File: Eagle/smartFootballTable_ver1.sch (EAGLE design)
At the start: 22 parts, among them IC1 LM2940CT, K1 ARK500/2

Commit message: Updated board with latest changes after soldering
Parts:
- removed J5: (no value), jumper:J2X2MM
- added JP1: (no value), jumper:JP2W
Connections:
- net +5V: now also JP1.1; no longer J5.1
- net GND: now also JP1.3; no longer J5.3
- net N$31: now also JP1.2; no longer J5.2
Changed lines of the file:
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@@
 </part>
 <part name="ARDUINO_NANO1" library="ArduinoNanoV30" deviceset="ARDUINO_NANO" device=""/>
-<part name="J5" library="jumper" deviceset="J2" device="X2MM"/>
 <part name="DIS_1" library="#PaJa_konektory" deviceset="PSH02-07" device="W"/>
 <part name="DIS_2" library="#PaJa_konektory" deviceset="PSH02-07" device="W"/>
@@
 <part name="TEST" library="#PaJa_prepinace" deviceset="P-B1720" device=""/>
 <part name="J1" library="con-jack" deviceset="JACK-PLUG" device="1"/>
+<part name="JP1" library="jumper" deviceset="JP2W" device=""/>
 </parts>
 <sheets>
@@
 </instance>
 <instance part="ARDUINO_NANO1" gate="G$1" x="-7.62" y="53.34" rot="R180"/>
-<instance part="J5" gate="G$1" x="-20.32" y="10.16" rot="R90"/>
 <instance part="DIS_1" gate="KON" x="55.88" y="71.12" rot="R270"/>
 <instance part="DIS_2" gate="KON" x="55.88" y="35.56" rot="R270"/>
@@
 <instance part="TEST" gate="TLAC" x="27.94" y="12.7"/>
 <instance part="J1" gate="G$1" x="-45.72" y="111.76"/>
+<instance part="JP1" gate="1" x="-20.32" y="10.16"/>
 </instances>
 <busses>
@@
 <wire x1="-12.7" y1="-2.54" x2="-12.7" y2="-5.08" width="0.1524" layer="91"/>
 <wire x1="-12.7" y1="-5.08" x2="-10.16" y2="-5.08" width="0.1524" layer="91"/>
-<pinref part="J5" gate="G$1" pin="3"/>
-<wire x1="-17.78" y1="7.62" x2="-17.78" y2="-5.08" width="0.1524" layer="91"/>
-<junction x="-17.78" y="-5.08"/>
 <pinref part="SENS_2" gate="KON" pin="6"/>
 <pinref part="SENS_2" gate="KON" pin="7"/>
 <junction x="-12.7" y="-5.08"/>
+<pinref part="JP1" gate="1" pin="3"/>
+<wire x1="-17.78" y1="7.62" x2="-17.78" y2="-2.54" width="0.1524" layer="91"/>
+<junction x="-17.78" y="-2.54"/>
 </segment>
 </net>
@@
 <wire x1="-25.4" y1="-2.54" x2="-25.4" y2="5.08" width="0.1524" layer="91"/>
 <wire x1="-25.4" y1="5.08" x2="-22.86" y2="5.08" width="0.1524" layer="91"/>
-<pinref part="J5" gate="G$1" pin="1"/>
-<wire x1="-22.86" y1="5.08" x2="-22.86" y2="7.62" width="0.1524" layer="91"/>
 <wire x1="-35.56" y1="-5.08" x2="-35.56" y2="-2.54" width="0.1524" layer="91"/>
 <wire x1="-35.56" y1="-2.54" x2="-25.4" y2="-2.54" width="0.1524" layer="91"/>
 <junction x="-25.4" y="-2.54"/>
 <pinref part="SENS_1" gate="KON" pin="1"/>
+<pinref part="JP1" gate="1" pin="1"/>
+<wire x1="-22.86" y1="5.08" x2="-22.86" y2="7.62" width="0.1524" layer="91"/>
 </segment>
 </net>
@@
 <pinref part="R3" gate="G$1" pin="2"/>
 <pinref part="R4" gate="G$1" pin="2"/>
-<wire x1="-33.02" y1="15.24" x2="-20.32" y2="15.24" width="0.1524" layer="91"/>
-<pinref part="J5" gate="G$1" pin="2"/>
-<wire x1="-20.32" y1="15.24" x2="0" y2="15.24" width="0.1524" layer="91"/>
-<wire x1="-20.32" y1="7.62" x2="-20.32" y2="15.24" width="0.1524" layer="91"/>
-<junction x="-20.32" y="15.24"/>
-</segment>
-</net>
+<wire x1="-33.02" y1="15.24" x2="-15.24" y2="15.24" width="0.1524" layer="91"/>
+<pinref part="JP1" gate="1" pin="2"/>
+<wire x1="-15.24" y1="15.24" x2="0" y2="15.24" width="0.1524" layer="91"/>
+<wire x1="-20.32" y1="7.62" x2="-20.32" y2="5.08" width="0.1524" layer="91"/>
+<wire x1="-20.32" y1="5.08" x2="-15.24" y2="5.08" width="0.1524" layer="91"/>
+<wire x1="-15.24" y1="5.08" x2="-15.24" y2="15.24" width="0.1524" layer="91"/>
+<junction x="-15.24" y="15.24"/>
+</segment>
+</net>

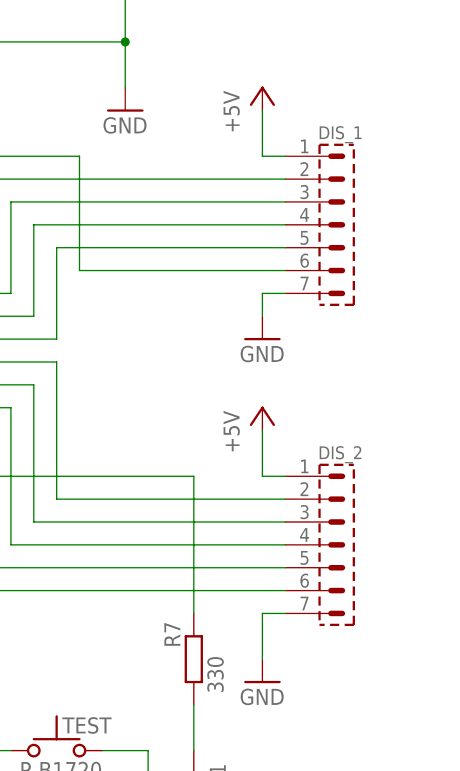
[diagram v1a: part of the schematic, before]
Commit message: Added pin description and started with PlatformIO
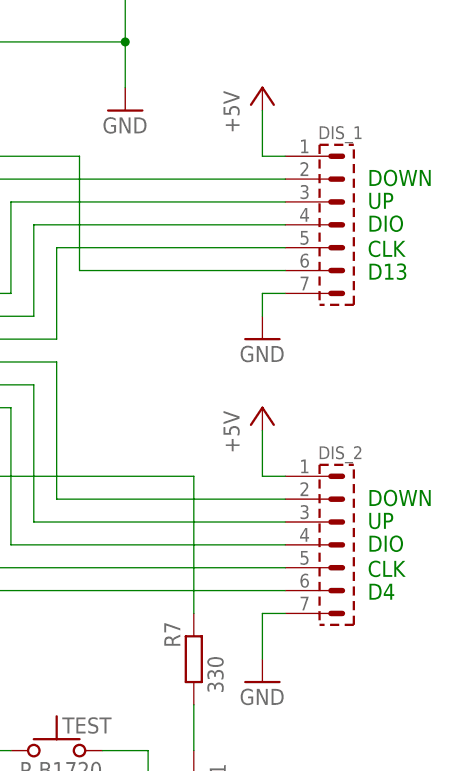
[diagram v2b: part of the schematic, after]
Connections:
- net D10 renamed DIS1_DIO
- net D5 renamed DIS2_CLK
- net D6 renamed DIS2_DIO
- net D7 renamed DIS2_UP
- net D8 renamed DIS2_DOWN
- net D9 renamed DIS1_CLK
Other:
- note added: "CLK"
- note added: "D13"
- note added: "D4"
- note added: "DIO"
- note added: "DOWN"
- note added: "UP"
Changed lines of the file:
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@@
 <sheet>
 <plain>
+<text x="62.484" y="32.004" size="1.778" layer="91">CLK</text>
+<text x="62.484" y="34.798" size="1.778" layer="91">DIO</text>
+<text x="62.484" y="39.878" size="1.778" layer="91">DOWN</text>
+<text x="62.484" y="37.338" size="1.778" layer="91">UP</text>
+<text x="62.484" y="75.438" size="1.778" layer="91">DOWN</text>
+<text x="62.484" y="72.898" size="1.778" layer="91">UP</text>
+<text x="62.484" y="70.358" size="1.778" layer="91">DIO</text>
+<text x="62.484" y="67.564" size="1.778" layer="91">CLK</text>
+<text x="62.484" y="29.464" size="1.778" layer="91">D4</text>
+<text x="62.484" y="65.024" size="1.778" layer="91">D13</text>
 </plain>
 <instances>
@@
 </segment>
 </net>
-<net name="D10" class="0">
+<net name="DIS1_DIO" class="0">
 <segment>
 <wire x1="25.4" y1="71.12" x2="53.34" y2="71.12" width="0.1524" layer="91"/>
@@
 </segment>
 </net>
-<net name="D9" class="0">
+<net name="DIS1_CLK" class="0">
 <segment>
 <wire x1="53.34" y1="68.58" x2="27.94" y2="68.58" width="0.1524" layer="91"/>
@@
 </segment>
 </net>
-<net name="D8" class="0">
+<net name="DIS2_DOWN" class="0">
 <segment>
 <wire x1="53.34" y1="40.64" x2="27.94" y2="40.64" width="0.1524" layer="91"/>
@@
 </segment>
 </net>
-<net name="D7" class="0">
+<net name="DIS2_UP" class="0">
 <segment>
 <wire x1="53.34" y1="38.1" x2="25.4" y2="38.1" width="0.1524" layer="91"/>
@@
 </segment>
 </net>
-<net name="D6" class="0">
+<net name="DIS2_DIO" class="0">
 <segment>
 <wire x1="53.34" y1="35.56" x2="22.86" y2="35.56" width="0.1524" layer="91"/>
@@
 </segment>
 </net>
-<net name="D5" class="0">
+<net name="DIS2_CLK" class="0">
 <segment>
 <wire x1="20.32" y1="48.26" x2="20.32" y2="33.02" width="0.1524" layer="91"/>
